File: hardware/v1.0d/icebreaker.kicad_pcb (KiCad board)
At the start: 4 copper layers, 73 x 37 mm, 191 parts, among them J1 Jumper, J10 Jumper, J11 Jumper, J12 Jumper, J13 Jumper, J14 Jumper, J15 Jumper, J16 Jumper, J17 Jumper, J18 Jumper, J19 Jumper, J2 Jumper, J20 Flash, J21 PMOD, J22 PMOD, J23 PMOD, J24 PMOD, J25 RGB Led, J26 5V AUX, J27 5V AUX, J28 CRESET, J29 Jumper, J3 Jumper, J30 Jumper, J31 RGB Led, J32 WS2812, J33 RGB Led, J34 SADD, J4 Jumper, J5 Jumper, J6 Jumper, J7 Jumper, J8 Jumper, J9 Jumper, P1 pkl_USB_OTG, P2 UP, P3 UP, P4 UP, P5 UP, P6 RAM_CS, Q1 BSS138, SW1 TACT, SW2 TACT, SW3 TACT, SW4 TACT, U1 93C46B-SOT-23-6, U2 3.3V, U3 1V2, U4 FT2232H, U5 W25Q, U6 ICE5LP4K-SG48, U7 12MHz

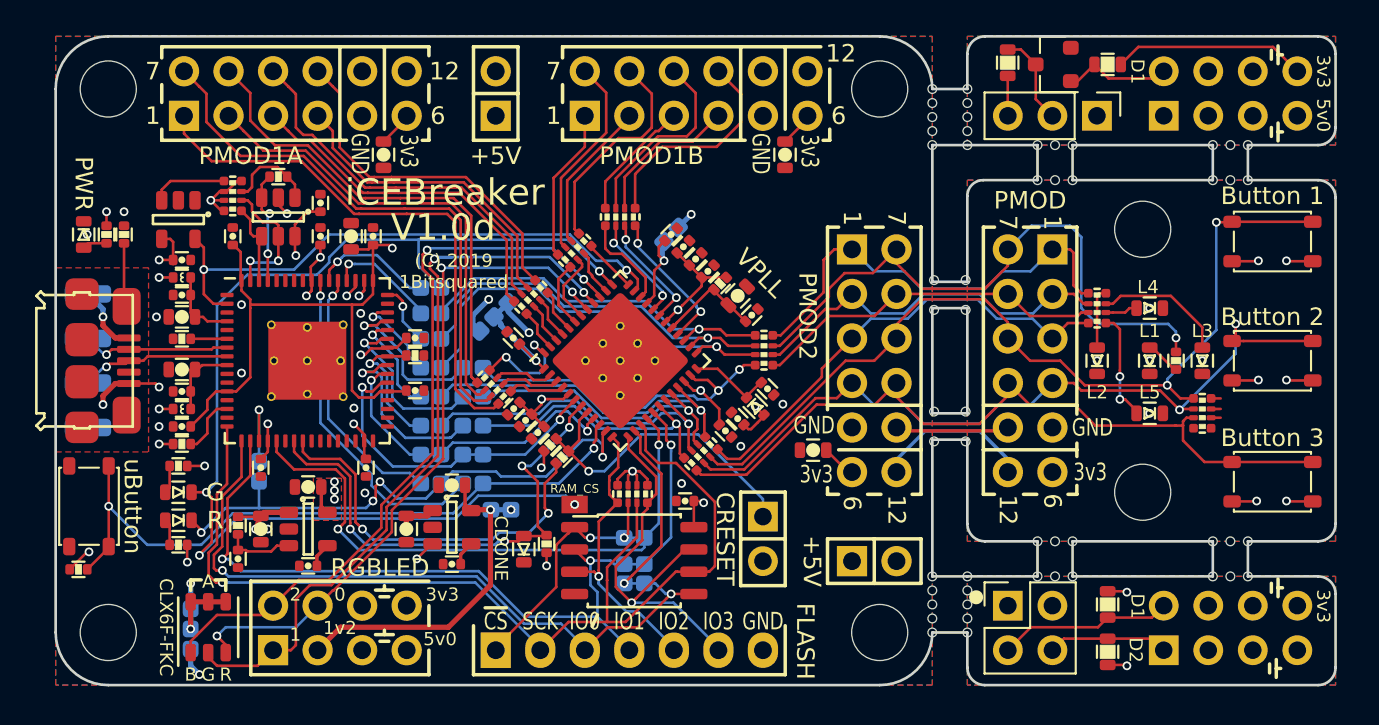
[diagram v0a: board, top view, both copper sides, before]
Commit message: Some more minor cleanups.
* Renamed ear data nets to match the RGB connector signal numbering
* Added graphics to make it clearer where the ear labels belong to
* Moved the 3v3 regulator via to increase the space between via drill
  hits
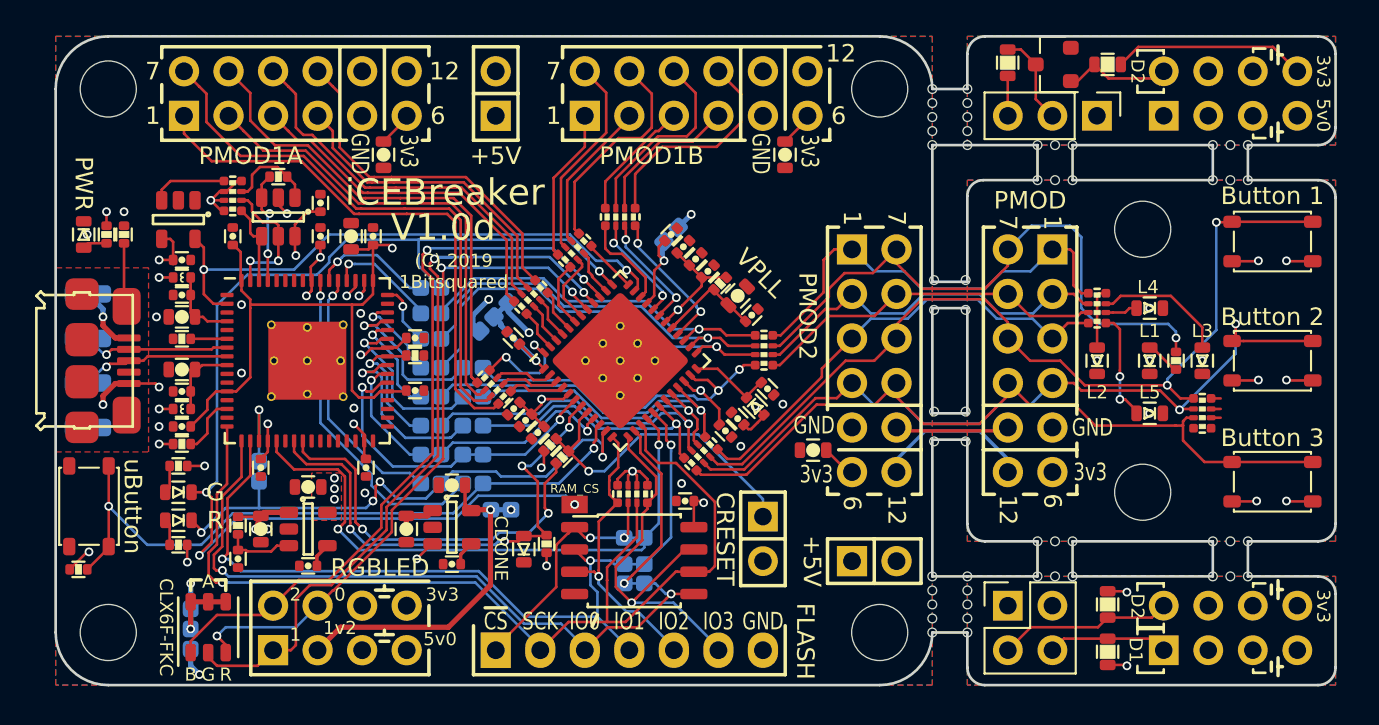
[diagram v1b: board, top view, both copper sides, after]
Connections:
- net /ET_O1 renamed /ET_O2
- net /ET_OD1 renamed /ET_OD2
- J33 pad 1: /EB_OD2 -> /EB_OD1
- J33 pad 2: /EB_OD1 -> /EB_OD2
- J34 pad 2: /EB_OD1 -> /EB_OD2
- J34 pad 4: /EB_OD2 -> /EB_OD1
- R28 pad 1: /EB_OD1 -> /EB_OD2
- R29 pad 1: /EB_OD2 -> /EB_OD1
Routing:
- net /EB_OD2: track 6.90 -> 9.94 mm
- net /EB_OD1: track 9.94 -> 6.90 mm
- net +3V3: track 69.5 -> 67.9 mm
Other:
- board text added: "D 2"
- board text removed: "D 1"

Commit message: Very minor trace adjustments to make things look prettier.
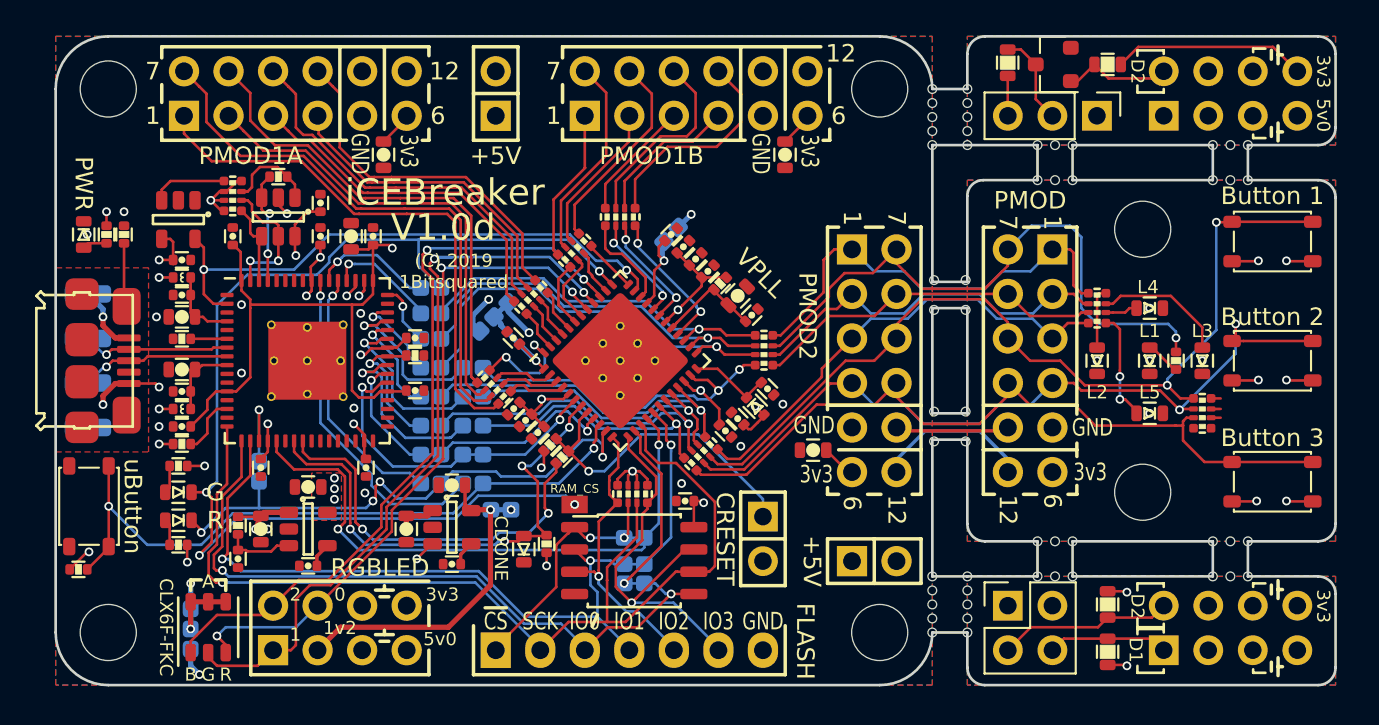
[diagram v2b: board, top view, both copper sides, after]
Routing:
- net /P1B8x: track 12.5 -> 11.7 mm

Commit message: Replaced/added the null logo to the boards.
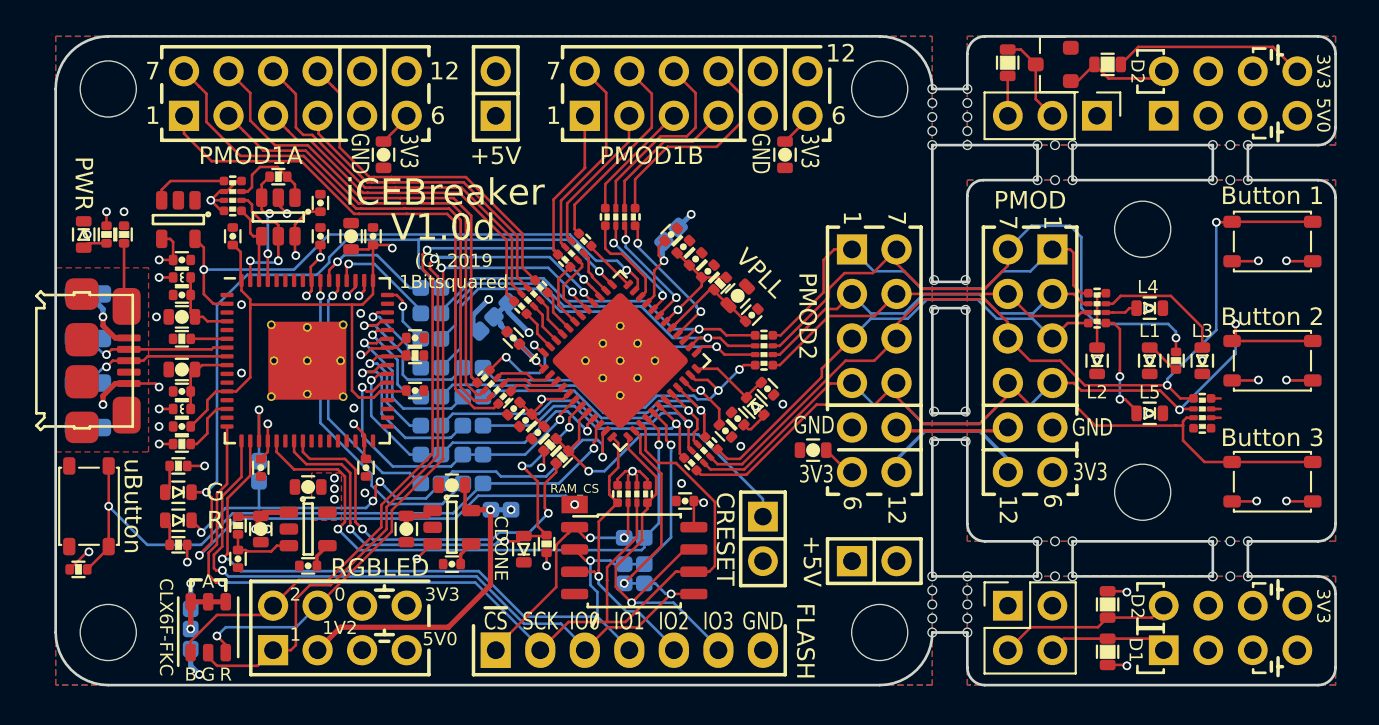
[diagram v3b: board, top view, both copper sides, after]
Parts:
- added REF**: null_Logo_SilkS_5mm, pkl_logos:null_Logo_SilkS_5mm, B.Cu at (42.2, 47.2)
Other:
- board text added: "1V2"
- board text added: "3V3 5V0"
- board text added: "5V0"
- board text added: "NULL"
- board text added: "RGB0 1V2"
- board text removed: "1v2"
- board text removed: "3v3"
- board text removed: "3v3 5v0"
- board text removed: "5v0"
- board text removed: "RGB0 1v2"

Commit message: Updated all design files to KiCad V8.0.6.
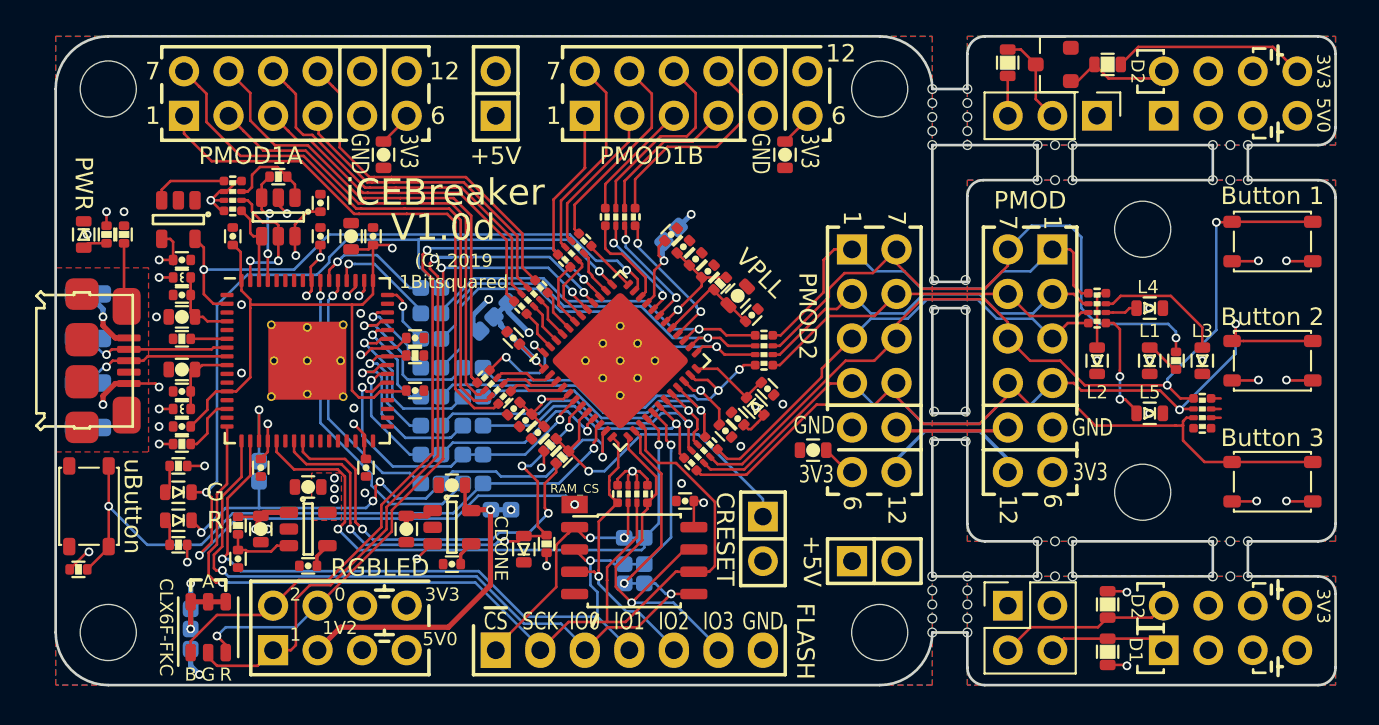
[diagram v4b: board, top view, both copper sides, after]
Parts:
- D2: value ~~800mVf -> ~800mVf
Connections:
- net /FLASH_~HLD~|~RST~|IO3 renamed /FLASH_~{HLD}|~{RST}|IO3
- net /FLASH_~WP~|IO2 renamed /FLASH_~{WP}|IO2
- net /xFIFO_~RD renamed /xFIFO_~{RD}
- net /xFIFO_~RXF renamed /xFIFO_~{RXF}
- net /xFIFO_~TXE renamed /xFIFO_~{TXE}
- net /xFIFO_~WR renamed /xFIFO_~{WR}
- net /~BUTTON renamed /~{BUTTON}
- net /~LEDG renamed /~{LEDG}
- net /~LEDR renamed /~{LEDR}
- net /~LED_RGB0 renamed /~{LED_RGB0}
- net /~LED_RGB1 renamed /~{LED_RGB1}
- net /~LED_RGB2 renamed /~{LED_RGB2}
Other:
- net class Default removed
- board text added: "~{CS}"
- board text removed: "~CS"
